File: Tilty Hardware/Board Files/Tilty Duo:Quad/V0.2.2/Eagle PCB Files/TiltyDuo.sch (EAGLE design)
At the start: 39 parts, among them U1 TEENSY_3.0_OUTER-PINS28-DIP_S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, U2 HC-09_BREAKOUT, U3 MPL3115A2LGA8, U4 LM2931, U5 MPU-6050, U6 HMC5883LSMD, U7 24LC08BT

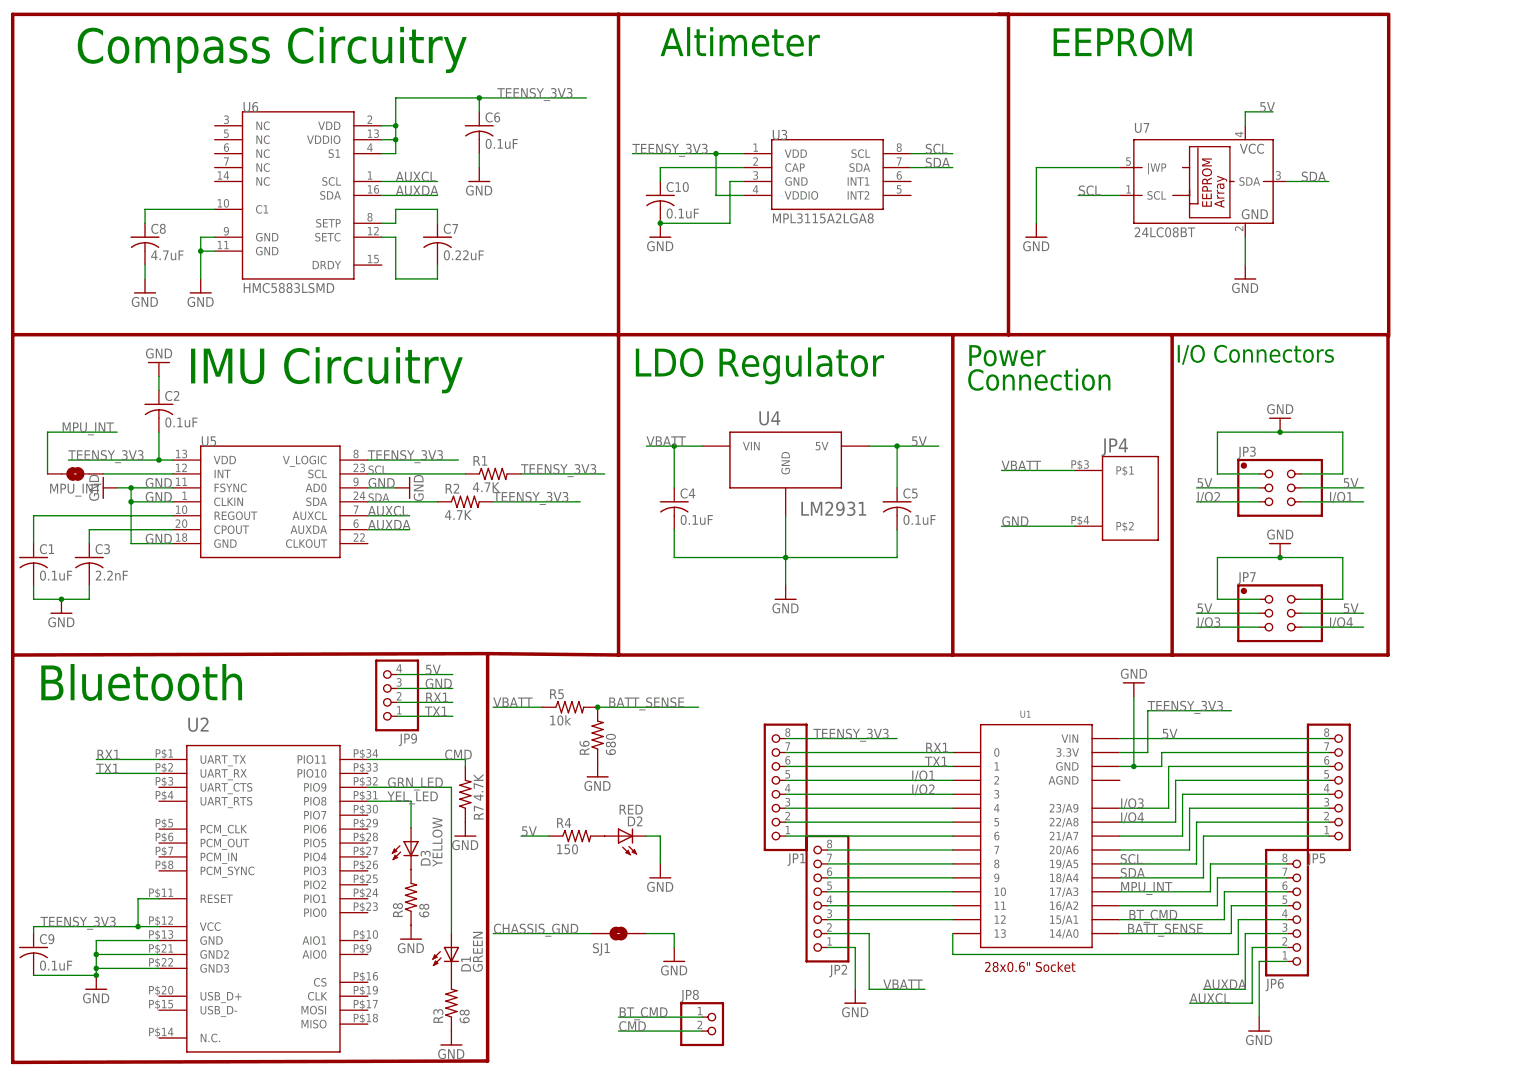
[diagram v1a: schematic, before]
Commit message: V 0.2.2 of the board and bluetoth arduino libraries updated
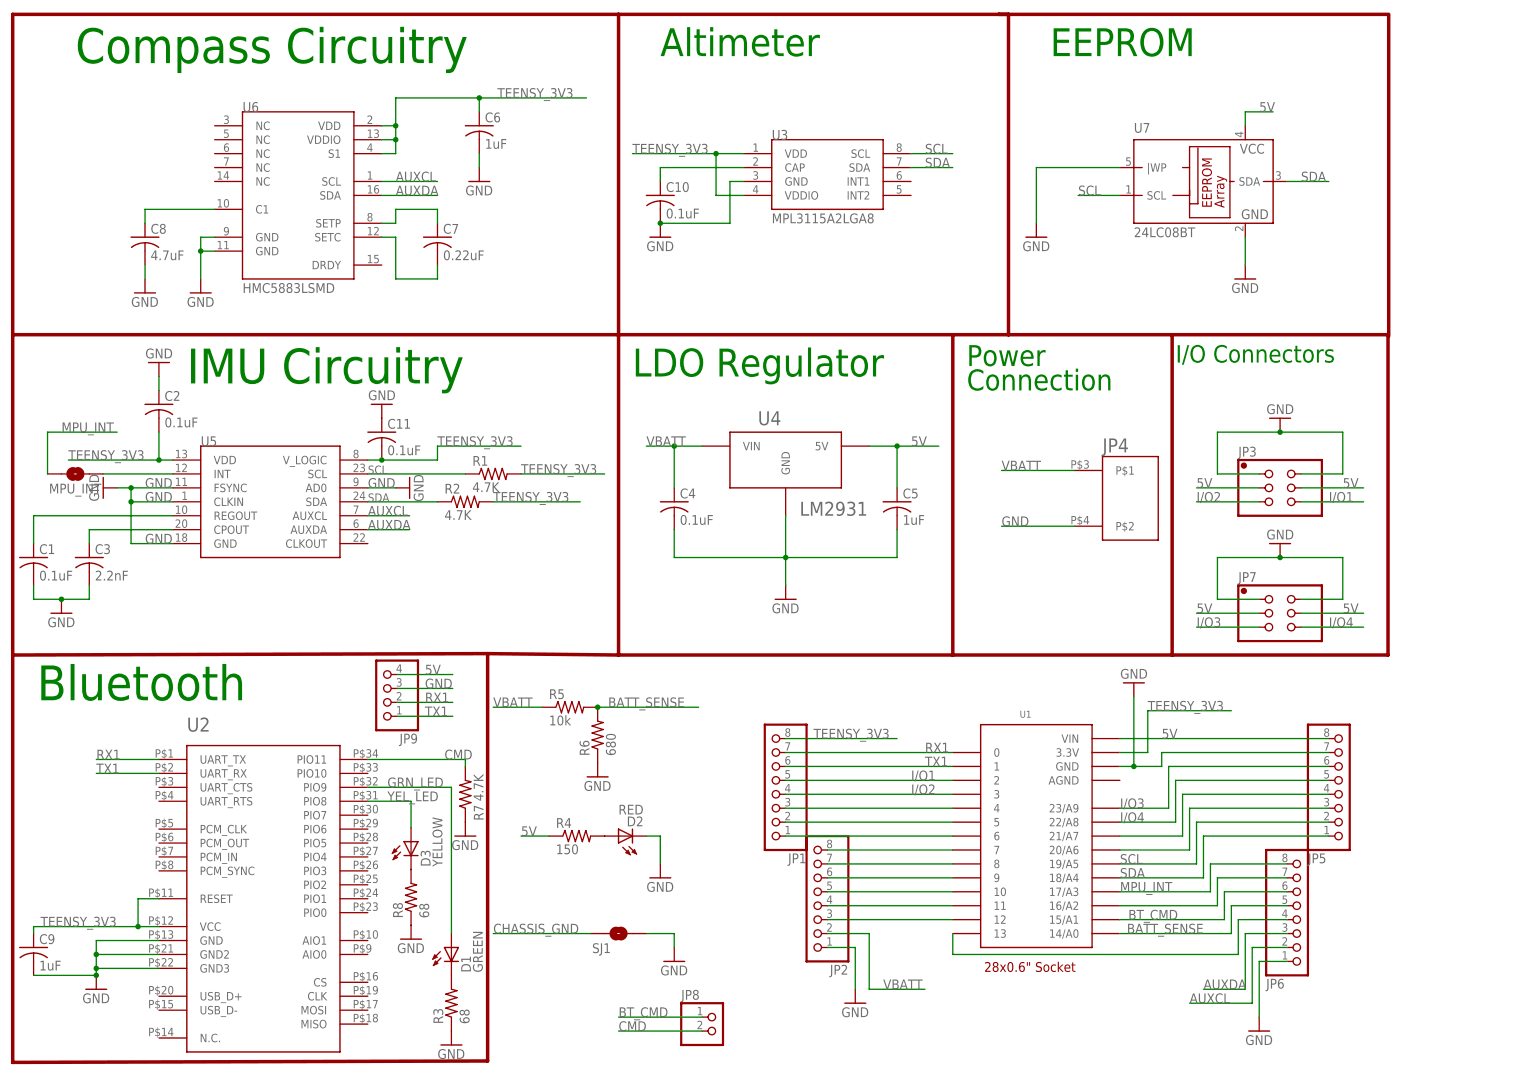
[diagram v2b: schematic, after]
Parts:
- added C11: 0.1uF, resistor:C-USC0603
- C5, C6, C9: value 0.1uF -> 1uF
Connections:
- net GND: now also C11.1
- net TEENSY_3V3: now also C11.2
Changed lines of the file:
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@@
 </part>
 <part name="C4" library="resistor" deviceset="C-US" device="C0603" value="0.1uF"/>
-<part name="C5" library="resistor" deviceset="C-US" device="C0603" value="0.1uF"/>
+<part name="C5" library="resistor" deviceset="C-US" device="C0603" value="1uF"/>
 <part name="U1" library="My Parts" deviceset="TEENSY_3.0_OUTER-PINS" device="28-DIP_SOCKET">
 <attribute name="COST" value="0.28"/>
@@
 <part name="C7" library="resistor" deviceset="C-US" device="C0603" value="0.22uF"/>
 <part name="C8" library="resistor" deviceset="C-US" device="C0603" value="4.7uF"/>
-<part name="C6" library="resistor" deviceset="C-US" device="C0603" value="0.1uF">
+<part name="C6" library="resistor" deviceset="C-US" device="C0603" value="1uF">
 <attribute name="RATED_VOLTAGE" value="2"/>
 </part>
@@
 <part name="R4" library="resistor" deviceset="R-US_" device="R0603" value="150"/>
 <part name="GND17" library="supply1" deviceset="GND" device=""/>
-<part name="C9" library="resistor" deviceset="C-US" device="C0603" value="0.1uF">
+<part name="C9" library="resistor" deviceset="C-US" device="C0603" value="1uF">
 <attribute name="RATED_VOLTAGE" value="2"/>
 </part>
@@
 <part name="GND22" library="SparkFun" deviceset="GND" device=""/>
 <part name="GND23" library="SparkFun" deviceset="GND" device=""/>
+<part name="C11" library="resistor" deviceset="C-US" device="C0603" value="0.1uF"/>
+<part name="GND24" library="supply1" deviceset="GND" device=""/>
 </parts>
 <sheets>
@@
 <instance part="GND22" gate="1" x="187.96" y="152.4"/>
 <instance part="GND23" gate="1" x="226.06" y="144.78"/>
+<instance part="C11" gate="G$1" x="68.58" y="116.84"/>
+<instance part="GND24" gate="1" x="68.58" y="121.92" rot="R180"/>
 </instances>
 <busses>
@@
 <pinref part="GND23" gate="1" pin="GND"/>
 </segment>
+<segment>
+<pinref part="C11" gate="G$1" pin="1"/>
+<pinref part="GND24" gate="1" pin="GND"/>
+</segment>
 </net>
 <net name="SCL" class="4">
@@
 <wire x1="93.98" y1="109.22" x2="109.22" y2="109.22" width="0.1524" layer="91"/>
 <label x="93.98" y="109.22" size="1.778" layer="95"/>
+<wire x1="78.74" y1="114.3" x2="93.98" y2="114.3" width="0.1524" layer="91"/>
+<label x="78.74" y="114.3" size="1.778" layer="95"/>
 </segment>
 <segment>
@@
 <wire x1="88.9" y1="104.14" x2="104.775" y2="104.14" width="0.1524" layer="91"/>
 <label x="88.9" y="104.14" size="1.778" layer="95"/>
-</segment>
-<segment>
-<pinref part="U5" gate="G$1" pin="V_LOGIC"/>
-<wire x1="66.04" y1="111.76" x2="82.55" y2="111.76" width="0.1524" layer="91"/>
-<label x="66.04" y="111.76" size="1.778" layer="95"/>
 </segment>
 <segment>
@@
 <segment>
 <pinref part="U3" gate="G$1" pin="VDD"/>
+<pinref part="U3" gate="G$1" pin="VDDIO"/>
 <wire x1="134.62" y1="167.64" x2="129.54" y2="167.64" width="0.1524" layer="91"/>
-<pinref part="U3" gate="G$1" pin="VDDIO"/>
 <wire x1="129.54" y1="167.64" x2="114.3" y2="167.64" width="0.1524" layer="91"/>
 <wire x1="134.62" y1="160.02" x2="129.54" y2="160.02" width="0.1524" layer="91"/>
@@
 <label x="147.32" y="60.96" size="1.778" layer="95"/>
 </segment>
-</net>
+<segment>
+<pinref part="U5" gate="G$1" pin="V_LOGIC"/>
+<pinref part="C11" gate="G$1" pin="2"/>
+<wire x1="66.04" y1="111.76" x2="68.58" y2="111.76" width="0.1524" layer="91"/>
+<wire x1="68.58" y1="111.76" x2="78.74" y2="111.76" width="0.1524" layer="91"/>
+<wire x1="78.74" y1="111.76" x2="78.74" y2="114.3" width="0.1524" layer="91"/>
+<junction x="68.58" y="111.76"/>
+</segment>
+</net>

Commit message: Software and Hardware update
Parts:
- added C12: 1uF, resistor:C-USC0603
- added SJ2, SJ3: (no value), SparkFun-Passives:SOLDERJUMPER_2WAYS
- C6: value 1uF -> 0.1uF
- C7, C8: ESR (none) -> <200mOhms
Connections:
- new net POW_I/O1: JP3.3, JP3.4, SJ2.2
- new net POW_I/O2: JP7.3, JP7.4, SJ3.2
- net 5V: now also SJ2.1, SJ3.1; no longer JP3.3, JP3.4, JP7.3, JP7.4
- net GND: now also C12.1
- net TEENSY_3V3: now also C12.2, SJ2.3, SJ3.3
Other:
- moved on the sheet: JP3, JP7

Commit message: Fixed a problem on the prototype PCB and added EEPROM testing code
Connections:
- net 5V: no longer U7.VCC
- net TEENSY_3V3: now also U7.VCC
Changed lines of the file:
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@@
 <label x="259.08" y="121.92" size="1.778" layer="95"/>
+</segment>
+<segment>
+<pinref part="U7" gate="G$1" pin="VCC"/>
+<wire x1="226.06" y1="172.72" x2="226.06" y2="175.26" width="0.1524" layer="91"/>
+<wire x1="226.06" y1="175.26" x2="231.14" y2="175.26" width="0.1524" layer="91"/>
+<label x="228.6" y="175.26" size="1.778" layer="95"/>
 </segment>
 </net>
@@
 </segment>
 <segment>
-<pinref part="U7" gate="G$1" pin="VCC"/>
-<wire x1="226.06" y1="172.72" x2="226.06" y2="175.26" width="0.1524" layer="91"/>
-<wire x1="226.06" y1="175.26" x2="231.14" y2="175.26" width="0.1524" layer="91"/>
-<label x="228.6" y="175.26" size="1.778" layer="95"/>
-</segment>
-<segment>
